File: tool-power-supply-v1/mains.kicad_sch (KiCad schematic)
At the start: 26 parts, among them J1 HB9500M-9.5-03P (AC IN: L N P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, J2 HB9500M-9.5-03P (AC OUT: L N 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, U1 IRM-90-12, U2 ACS712ELCTR-20A-T

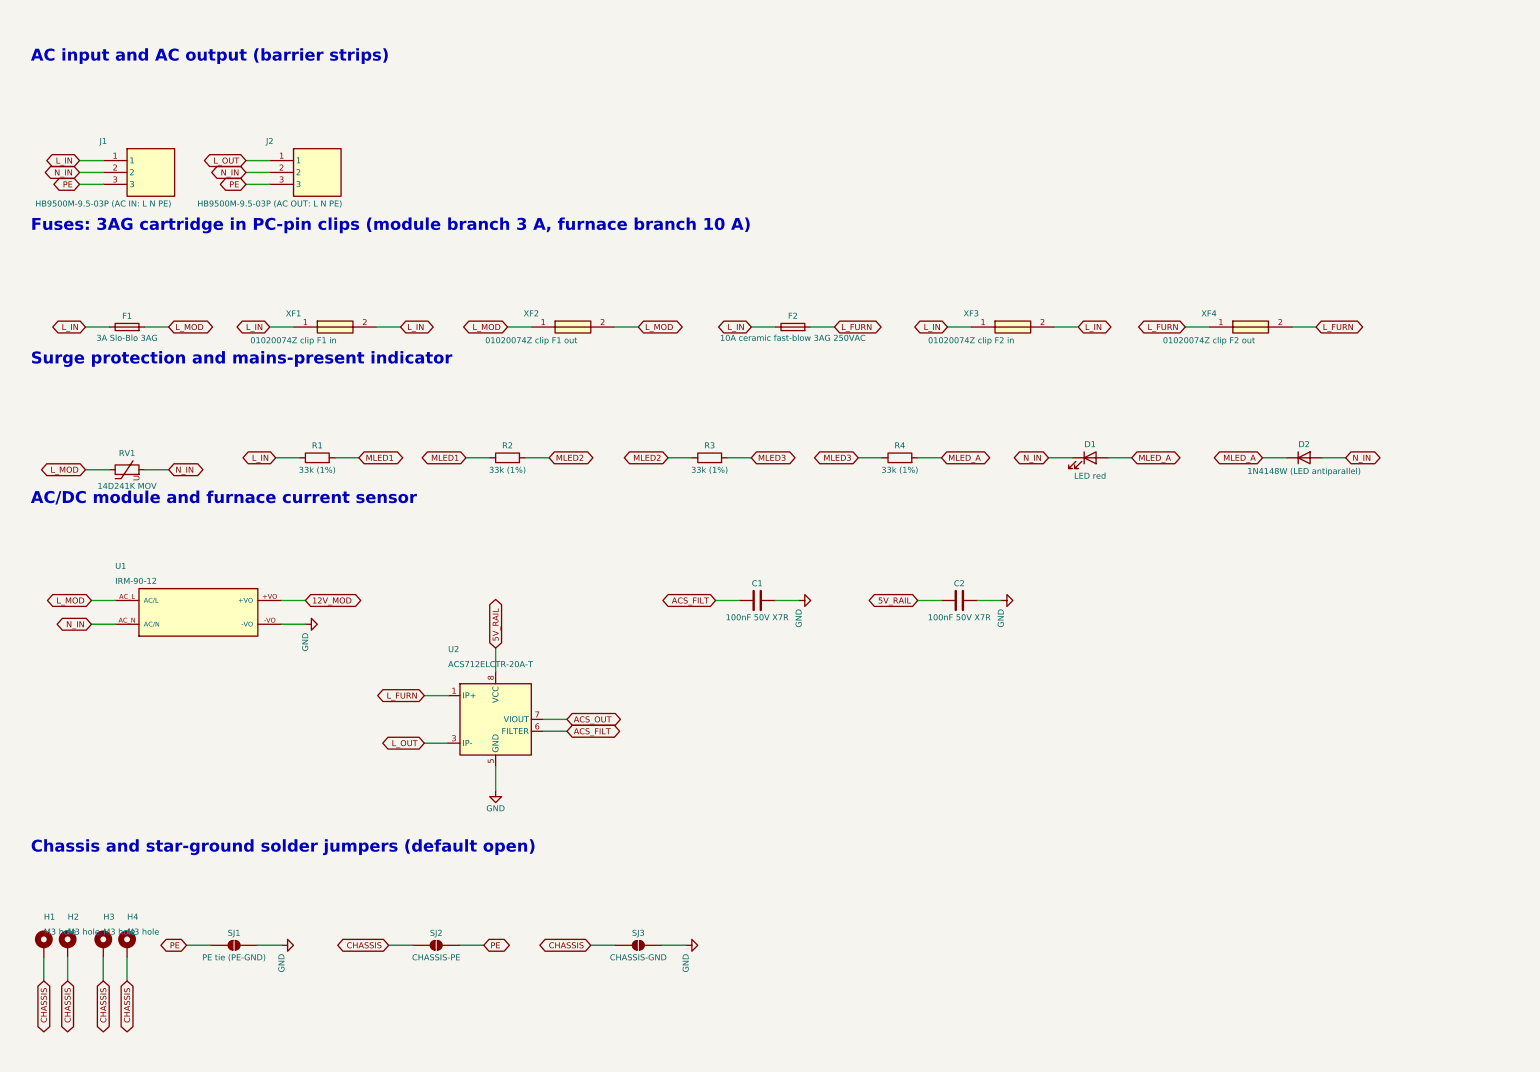
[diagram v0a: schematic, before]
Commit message: schematic update: cleaned up by using sheet labels and busses, updated documentation
Co-Authored-By: Claude Sonnet 5.5 <noreply@anthropic.com>
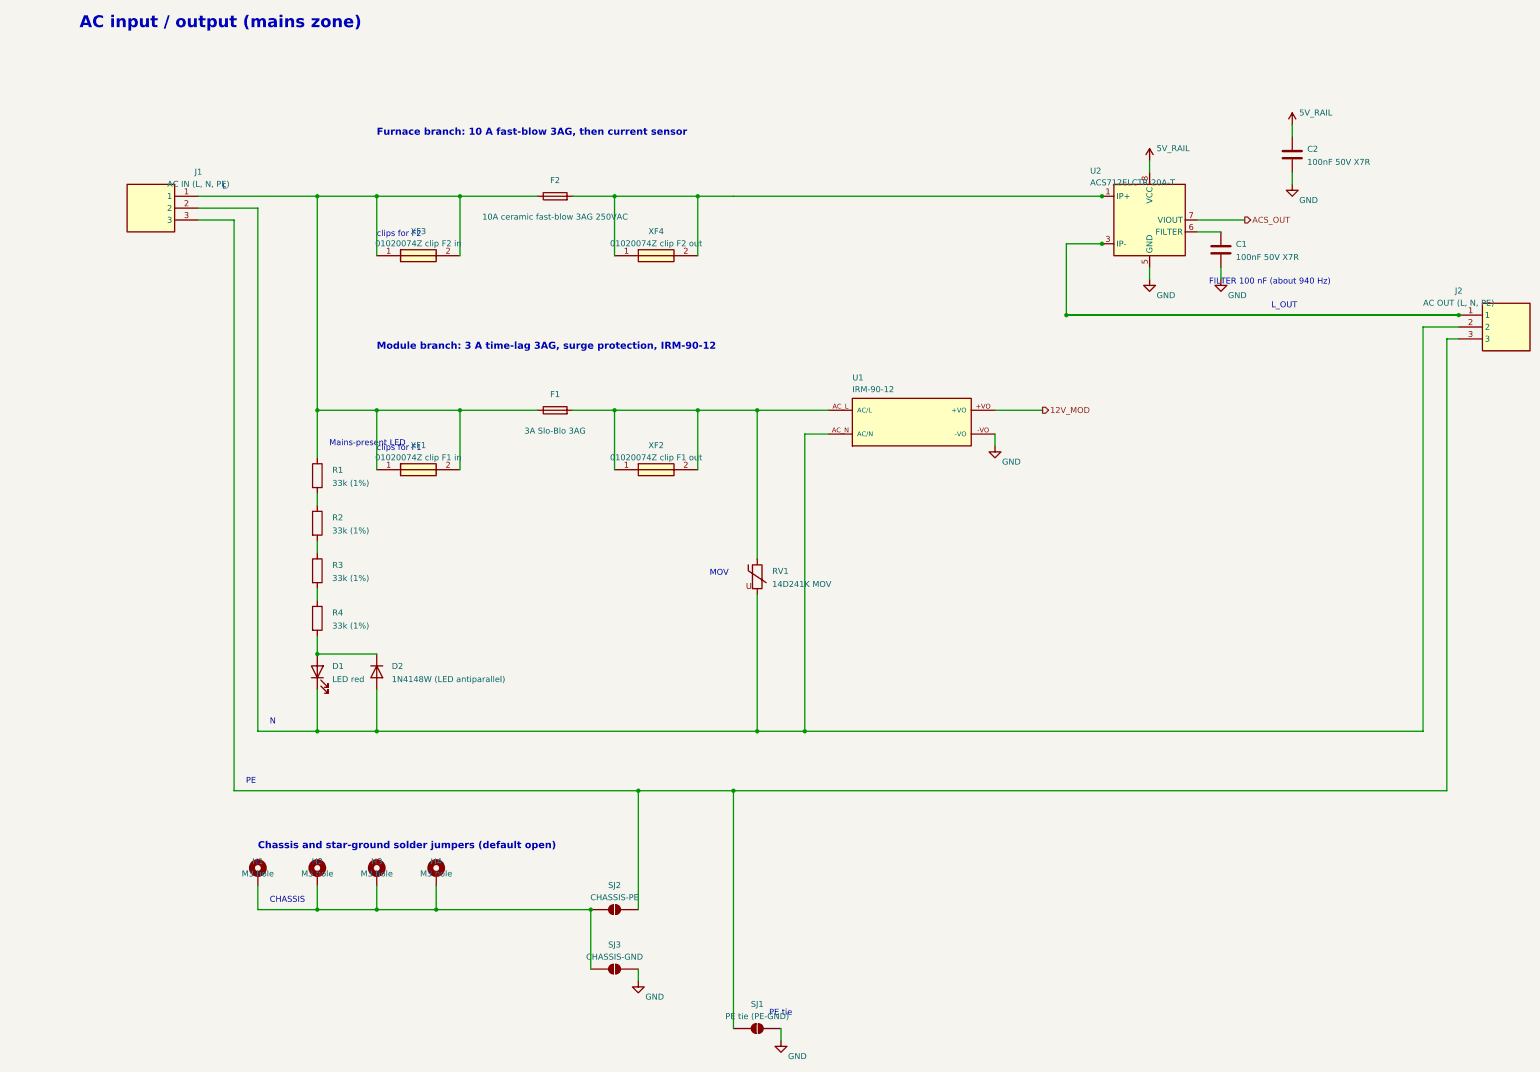
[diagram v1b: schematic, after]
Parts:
- J1: value HB9500M-9.5-03P (AC IN: L N PE) -> AC IN (L, N, PE)
- J2: value HB9500M-9.5-03P (AC OUT: L N PE) -> AC OUT (L, N, PE)
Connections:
- net ACS_FILT: no longer names the net of C1.1, U2.6 (FILTER)
- net CHASSIS: no longer names the net of H1.1, H2.1, H3.1, H4.1, SJ2.1 (A), SJ3.1 (A)
- net L_FURN: no longer names the net of F2.2, U2.1 (IP+), U2.2 (IP+), XF4.1, XF4.2
- net L_IN: no longer names the net of F1.1, F2.1, J1.1, R1.1, XF1.1, XF1.2, XF3.1, XF3.2
- net L_MOD: no longer names the net of F1.2, RV1.1, U1.AC_L (AC/L), XF2.1, XF2.2
- net L_OUT: no longer names the net of J2.1, U2.3 (IP-), U2.4 (IP-)
- net MLED1: no longer names the net of R1.2, R2.1
- net MLED2: no longer names the net of R2.2, R3.1
- net MLED3: no longer names the net of R3.2, R4.1
- net MLED_A: no longer names the net of D1.2 (A), D2.1 (K), R4.2
- net N_IN: no longer names the net of D1.1 (K), D2.2 (A), J1.2, J2.2, RV1.2, U1.AC_N (AC/N)
- net PE: no longer names the net of J1.3, J2.3, SJ1.1 (A), SJ2.2 (B)
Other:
- note added: "AC input / output (mains zone)"
- note added: "CHASSIS"
- note added: "FILTER 100 nF (about 940 Hz)"
- note added: "Furnace branch: 10 A fast-blow 3AG, then current sensor"
- note added: "L"
- note added: "L_OUT"
- note added: "MOV"
- note added: "Mains-present LED"
- note added: "Module branch: 3 A time-lag 3AG, surge protection, IRM-90-12"
- note added: "N"
- note added: "PE"
- note added: "PE tie"
- note added: "clips for F1"
- note added: "clips for F2"
- note removed: "AC input and AC output (barrier strips)"
- note removed: "AC/DC module and furnace current sensor"
- note removed: "Fuses: 3AG cartridge in PC-pin clips (module branch 3 A, furnace branch 10 A)"
- note removed: "Surge protection and mains-present indicator"
